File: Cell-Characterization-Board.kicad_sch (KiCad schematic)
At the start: 5 parts, among them IC2 INA4180A2IPWR, SW1 SW_Push, U1 ESP32-S3-WROOM-1

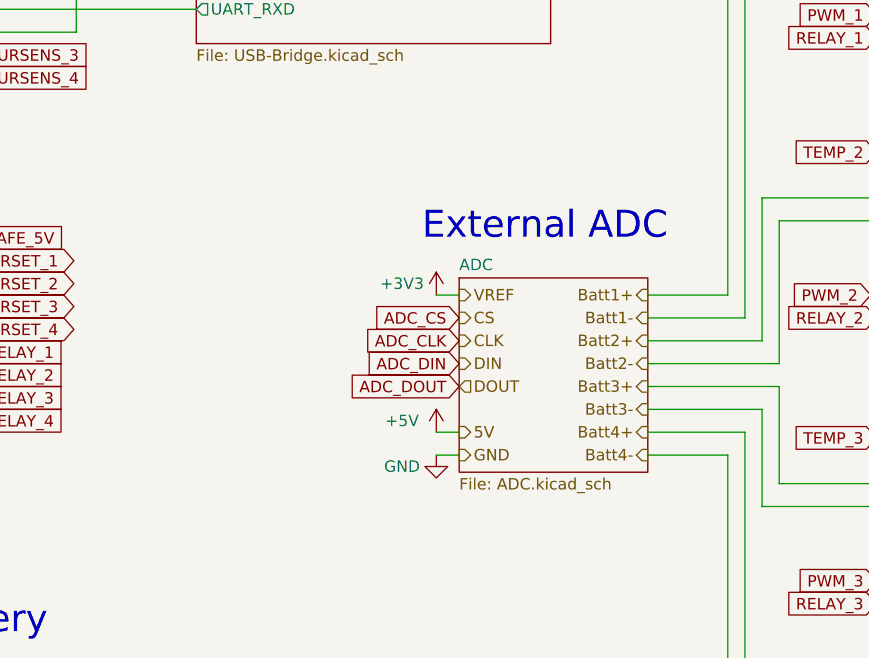
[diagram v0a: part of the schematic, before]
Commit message: Updated the ADC, whoopsies
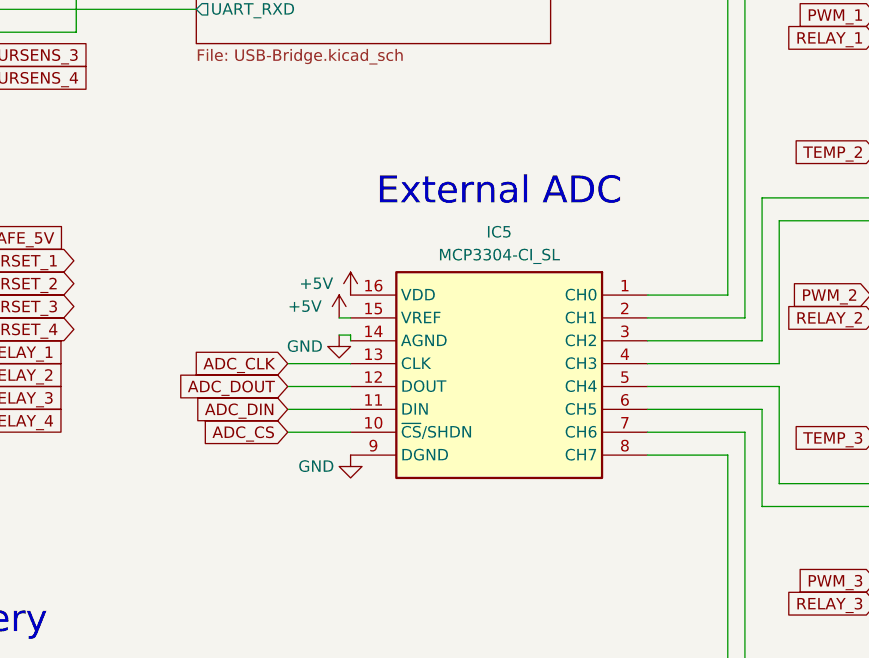
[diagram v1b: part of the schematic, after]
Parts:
- added IC5: MCP3304-CI_SL, SOIC127P600X175-16N, symbol MCP3304-CI_SL:MCP3304-CI_SL
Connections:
- net +5V: now also IC5.15 (VREF), IC5.16 (VDD)
- net ADC_CLK: now also IC5.13 (CLK)
- net ADC_CS: now also IC5.10 (~{CS}/SHDN)
- net ADC_DIN: now also IC5.11 (DIN)
- net ADC_DOUT: now also IC5.12 (DOUT)
- net GND: now also IC5.14 (AGND), IC5.9 (DGND)
- new net Cell1/Batt+: IC5.1 (CH0)
- new net Cell1/Batt-: IC5.2 (CH1)
- new net Cell2/Batt+: IC5.3 (CH2)
- new net Cell2/Batt-: IC5.4 (CH3)
- new net Cell3/Batt+: IC5.5 (CH4)
- new net Cell3/Batt-: IC5.6 (CH5)
- new net Cell4/Batt+: IC5.7 (CH6)
- new net Cell4/Batt-: IC5.8 (CH7)
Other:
- removed sheet ADC
